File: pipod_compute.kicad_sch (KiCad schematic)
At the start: 2 parts

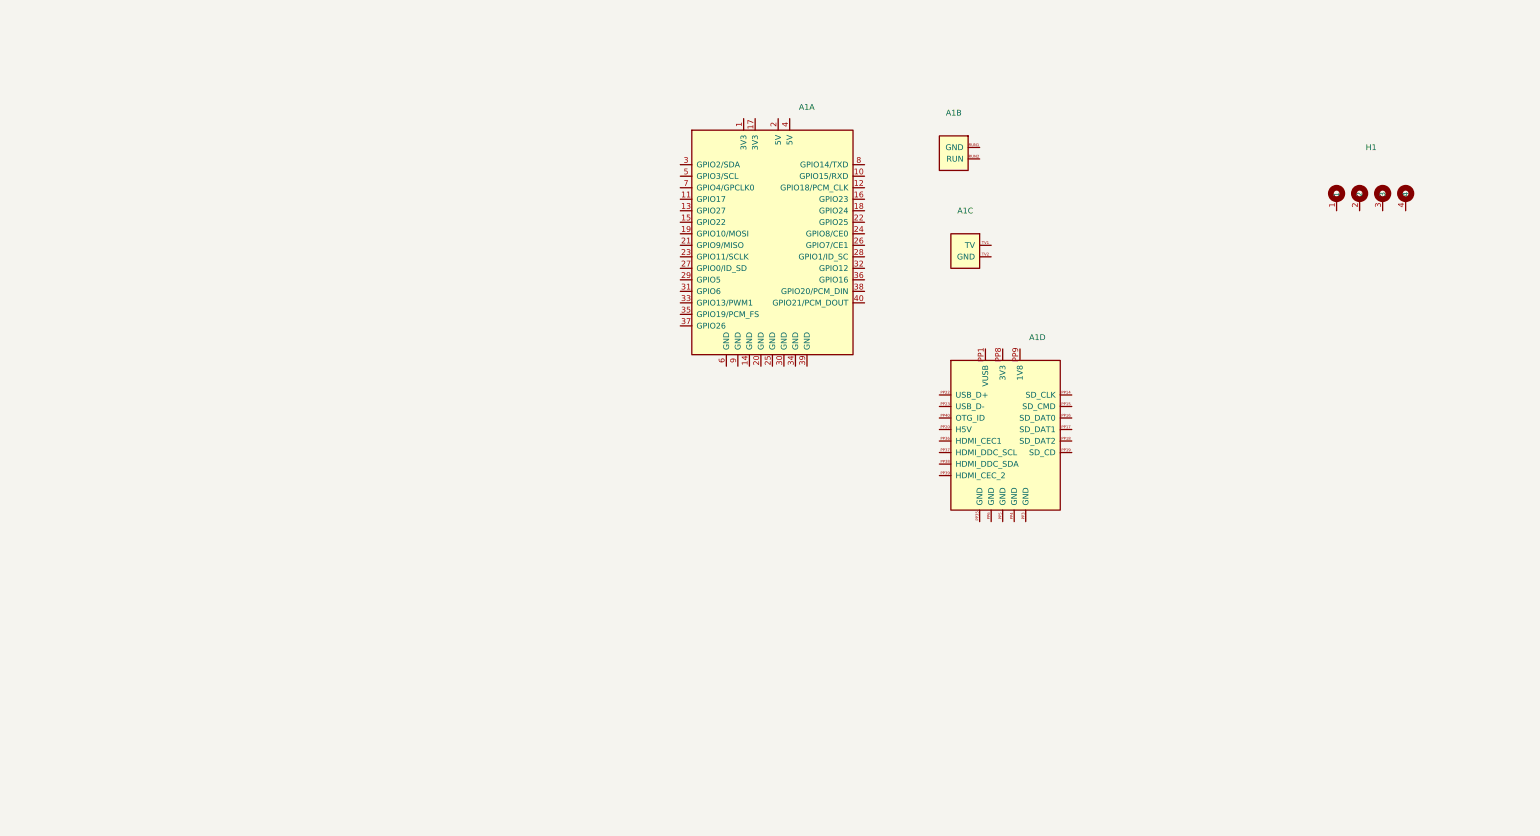
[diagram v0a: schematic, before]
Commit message: layout: cleanup silkscreen, add bootloader buttons
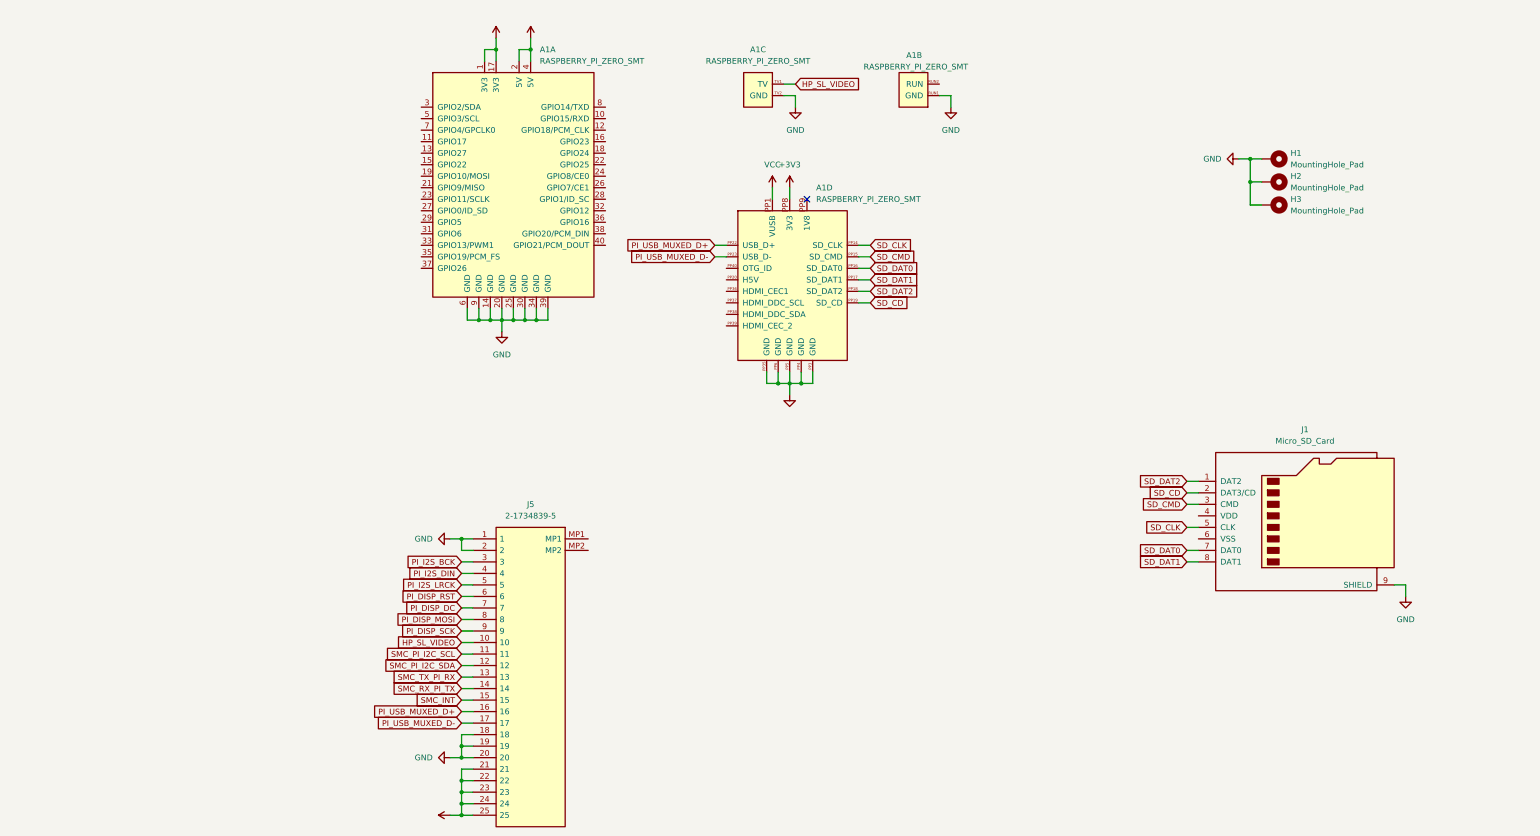
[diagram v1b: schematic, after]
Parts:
- removed H1: (no value), symbol pipod_hw:MountingHole_PiPod
- added H1, H2, H3: MountingHole_Pad, MountingHole:MountingHole_2.2mm_M2_DIN965_Pad, symbol Mechanical:MountingHole_Pad
- added J1: Micro_SD_Card, Gigahawk:microSD_HC_Hirose_DM3AT-SF-PEJM5, symbol Connector:Micro_SD_Card
- added J5: 2-1734839-5, Gigahawk:217348395, symbol gigahawk:2-1734839-5
- A1: value (none) -> RASPBERRY_PI_ZERO_SMT; footprint (none) -> Gigahawk:RASPI_ZERO_1_3_SMT_LOW_PROFILE
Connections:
- net HP_SL_VIDEO: now reaches A1.TV1 (TV)
- net HP_SL_VIDEO: now also J5.10
- net GND: now reaches A1.TV2 (GND)
- net GND: now also A1.14 (GND), A1.20 (GND), A1.25 (GND), A1.30 (GND), A1.34 (GND), A1.39 (GND), A1.6 (GND), A1.9 (GND), A1.PP3 (GND), A1.PP35 (GND), A1.PP4 (GND), A1.PP5 (GND), A1.PP6 (GND), A1.RUN1 (GND), H1.1, H2.1, H3.1, J1.9 (SHIELD), J5.1, J5.18, J5.19, J5.2, J5.20
- net VCC: now reaches A1.PP1 (VUSB)
- net VCC: now also A1.2 (5V), A1.4 (5V), J5.21, J5.22, J5.23, J5.24, J5.25
- net SD_CLK: now reaches A1.PP14 (SD_CLK)
- net SD_CLK: now also J1.5 (CLK)
- net SD_CMD: now reaches A1.PP15 (SD_CMD)
- net SD_CMD: now also J1.3 (CMD)
- net SD_DAT0: now reaches A1.PP16 (SD_DAT0)
- net SD_DAT0: now also J1.7 (DAT0)
- net SD_DAT1: now reaches A1.PP17 (SD_DAT1)
- net SD_DAT1: now also J1.8 (DAT1)
- net SD_DAT2: now reaches A1.PP18 (SD_DAT2)
- net SD_DAT2: now also J1.1 (DAT2)
- net SD_CD: now reaches A1.PP19 (SD_CD)
- net SD_CD: now also J1.2 (DAT3/CD)
- net PI_USB_MUXED_D+: now reaches A1.PP22 (USB_D+)
- net PI_USB_MUXED_D+: now also J5.16
- net PI_USB_MUXED_D-: now reaches A1.PP23 (USB_D-)
- net PI_USB_MUXED_D-: now also J5.17
- net +3V3: now reaches A1.PP8 (3V3)
- net +3V3: now also A1.1 (3V3), A1.17 (3V3)
- new net PI_DISP_DC: J5.7
- new net PI_DISP_MOSI: J5.8
- new net PI_DISP_RST: J5.6
- new net PI_DISP_SCK: J5.9
- new net PI_I2S_BCK: J5.3
- new net PI_I2S_DIN: J5.4
- new net PI_I2S_LRCK: J5.5
- new net SMC_INT: J5.15
- new net SMC_PI_I2C_SCL: J5.11
- new net SMC_PI_I2C_SDA: J5.12
- new net SMC_RX_PI_TX: J5.14
- new net SMC_TX_PI_RX: J5.13
- no-connect marks 0 -> 1
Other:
- moved on the sheet: A1A, A1B, A1C, A1D

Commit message: compute: finish layout and routing
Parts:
- added C1: (no value), symbol Device:C_Small
- added D1: (no value), symbol Device:LED
- added J?: S7041-42R, Gigahawk:S7041-42R, symbol gigahawk:S7041-42R
- added J?: (no value), symbol gigahawk:S7041-42R
- added R1, R2: (no value), symbol Device:R_Small
- added TP1, TP10, TP11, TP12, TP13, TP14, TP15, TP16, TP17, TP18, TP19, TP2, TP20, TP21, TP22, TP23, TP24, TP3, TP4, TP5, TP6, TP7, TP8, TP9: TestPoint, TestPoint:TestPoint_Pad_D1.5mm, symbol Connector:TestPoint
- J1: symbol Connector:Micro_SD_Card -> Connector:Micro_SD_Card_Det_Hirose_DM3AT
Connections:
- net +3V3: now also J1.4 (VDD), C1.2, R1.2, TP3.1
- net GND: now also J1.10 (DET_A), J1.11 (SHIELD), J1.6 (VSS), C1.1, J?.1, J?.1, R2.1, TP1.1; no longer J1.9 (SHIELD)
- net HP_SL_VIDEO: now also TP11.1
- net PI_DISP_DC: now also A1.18 (GPIO24), TP14.1
- net PI_DISP_MOSI: now also A1.19 (GPIO10/MOSI), TP13.1
- net PI_DISP_RST: now also A1.22 (GPIO25), TP15.1
- net PI_DISP_SCK: now also A1.23 (GPIO11/SCLK), TP12.1
- net PI_I2S_BCK: now also A1.12 (GPIO18/PCM_CLK), TP18.1
- net PI_I2S_DIN: now also A1.40 (GPIO21/PCM_DOUT), TP17.1
- net PI_I2S_LRCK: now also A1.35 (GPIO19/PCM_FS), TP16.1
- net SD_CD: now also TP23.1
- net SD_CLK: now also TP21.1
- net SD_CMD: now also TP22.1
- net SD_DAT0: now also TP20.1
- net SD_DAT1: now also TP19.1
- net SD_DAT2: now also TP24.1
- net SMC_INT: now also A1.16 (GPIO23), TP6.1
- net SMC_PI_I2C_SCL: now also A1.5 (GPIO3/SCL), TP10.1
- net SMC_PI_I2C_SDA: now also A1.3 (GPIO2/SDA), TP9.1
- net SMC_RX_PI_TX: now also A1.8 (GPIO14/TXD), J5.13, TP8.1; no longer J5.14
- net SMC_TX_PI_RX: now also A1.10 (GPIO15/RXD), J5.14, TP7.1; no longer J5.13
- net VCC: now also TP2.1; no longer A1.PP1 (VUSB)
- net at A1.11 (GPIO17): now also D1.2 (A), TP4.1
- net SD_DET: now reaches A1.29 (GPIO5)
- net SD_DET: now also J1.9 (DET_B), R1.1, TP5.1
- new net: D1.1 (K), R2.2
- no-connect marks 1 -> 15
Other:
- moved on the sheet: A1A, A1B, A1C, A1D

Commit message: ci: prepare files for CI
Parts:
- C1: value (none) -> 10u; footprint (none) -> Capacitor_SMD:C_0805_2012Metric
- D1: value (none) -> GRN; footprint (none) -> LED_SMD:LED_0805_2012Metric
- J2: renamed from J?; value (none) -> S7041-42R; footprint (none) -> Gigahawk:S7041-42R
- R1: value (none) -> 10k; footprint (none) -> Resistor_SMD:R_0805_2012Metric
- R2: value (none) -> 470R; footprint (none) -> Resistor_SMD:R_0805_2012Metric
- gave numbers to parts that had none: 1
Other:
- note added: "Mounting Holes"
- note added: "Shielding Clips"
- title: (none) -> piPod Compute Board
- moved on the sheet: J2, J3

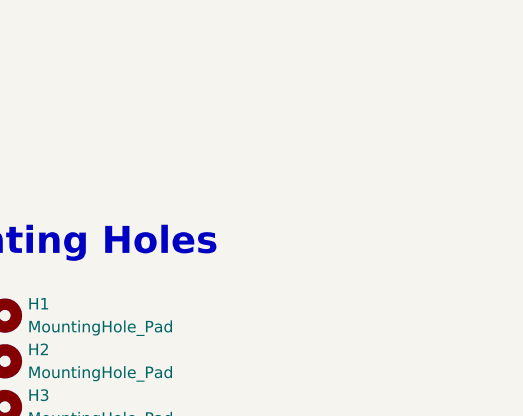
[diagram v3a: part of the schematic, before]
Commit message: layout: add OSHW logo, change version text to masked copper
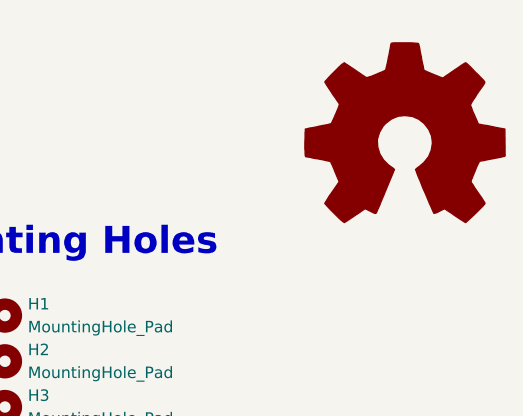
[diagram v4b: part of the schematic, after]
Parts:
- added LOGO1: (no value), symbol Graphic:Logo_Open_Hardware_Large
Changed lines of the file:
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@@
     (pin "1")
+  )
+  (symbol (lib_id "Graphic:Logo_Open_Hardware_Large") (at 267.97 27.94 0) (unit 1)
+    (in_bom yes) (on_board yes) (fields_autoplaced)
+    (property "Reference" "LOGO1" (id 0) (at 267.97 15.24 0)
+      (effects (font (size 1.27 1.27)) hide)
+    )
+    (property "Value" "" (id 1) (at 267.97 38.1 0)
+      (effects (font (size 1.27 1.27)) hide)
+    )
+    (property "Footprint" "" (id 2) (at 267.97 27.94 0)
+      (effects (font (size 1.27 1.27)) hide)
+    )
+    (property "Datasheet" "~" (id 3) (at 267.97 27.94 0)
+      (effects (font (size 1.27 1.27)) hide)
+    )
   )
   (symbol (lib_id "Device:R_Small") (at 27.94 43.18 90) (unit 1)
@@
       (reference "J5") (unit 1) (value "2-1734839-5") (footprint "Gigahawk:217348395")
     )
+    (path "/2dc8ec45-12c1-425a-8d7d-7071080501b5"
+      (reference "LOGO1") (unit 1) (value "Logo_Open_Hardware_Large") (footprint "Gigahawk:OSHW-Logo2_9.8x8mm_Mask")
+    )
     (path "/ea380145-c77c-4482-81f2-b2fdbe1fe607"

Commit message: compute: fill out bom columns
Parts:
- J1: Digikey Part (none) -> HR1964CT-ND; Digikey Price/Stock (none) -> https://www.digikey.ca/en/products/detail/hirose-electric-c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; JLC Part (none) -> Extended Part; LCSC Part (none) -> C114218; Manufacturer (none) -> Hirose Electric Co Ltd; Manufacturer Part (none) -> DM3AT-SF-PEJM5; Mouser Part (none) -> 798-DM3AT-SF-PEJM5; Mouser Price/Stock (none) -> https://www.mouser.ca/ProductDetail/Hirose-Connector/DM3AT-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
- LOGO1: value (none) -> Logo_Open_Hardware_Large; footprint (none) -> Gigahawk:OSHW-Logo2_9.8x8mm_Mask
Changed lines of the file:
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@@
       (effects (font (size 1.27 1.27)) hide)
     )
-    (property "Value" "" (id 1) (at 267.97 38.1 0)
-      (effects (font (size 1.27 1.27)) hide)
-    )
-    (property "Footprint" "" (id 2) (at 267.97 27.94 0)
+    (property "Value" "Logo_Open_Hardware_Large" (id 1) (at 267.97 38.1 0)
+      (effects (font (size 1.27 1.27)) hide)
+    )
+    (property "Footprint" "Gigahawk:OSHW-Logo2_9.8x8mm_Mask" (id 2) (at 267.97 27.94 0)
       (effects (font (size 1.27 1.27)) hide)
     )
@@
       (effects (font (size 1.27 1.27)) hide)
     )
+    (property "Description" "10 (8 + 2) Position Card Connector Secure Digital - microSD™ Surface Mount, Right Angle Gold" (id 4) (at 228.6 125.73 0)
+      (effects (font (size 1.27 1.27)) hide)
+    )
+    (property "Digikey Part" "HR1964CT-ND" (id 5) (at 228.6 125.73 0)
+      (effects (font (size 1.27 1.27)) hide)
+    )
+    (property "Digikey Price/Stock" "https://www.digikey.ca/en/products/detail/hirose-electric-co-ltd/DM3AT-SF-PEJM5/2533565" (id 6) (at 228.6 125.73 0)
+      (effects (font (size 1.27 1.27)) hide)
+    )
+    (property "JLC Part" "Extended Part" (id 7) (at 228.6 125.73 0)
+      (effects (font (size 1.27 1.27)) hide)
+    )
+    (property "LCSC Part" "C114218" (id 8) (at 228.6 125.73 0)
+      (effects (font (size 1.27 1.27)) hide)
+    )
+    (property "Manufacturer" "Hirose Electric Co Ltd" (id 9) (at 228.6 125.73 0)
+      (effects (font (size 1.27 1.27)) hide)
+    )
+    (property "Manufacturer Part" "DM3AT-SF-PEJM5" (id 10) (at 228.6 125.73 0)
+      (effects (font (size 1.27 1.27)) hide)
+    )
+    (property "Mouser Part" "798-DM3AT-SF-PEJM5" (id 11) (at 228.6 125.73 0)
+      (effects (font (size 1.27 1.27)) hide)
+    )
+    (property "Mouser Price/Stock" "https://www.mouser.ca/ProductDetail/Hirose-Connector/DM3AT-SF-PEJM5?qs=LZSZKJVF%252B2WTDKp%252BR7IYAQ%3D%3D" (id 12) (at 228.6 125.73 0)
+      (effects (font (size 1.27 1.27)) hide)
+    )

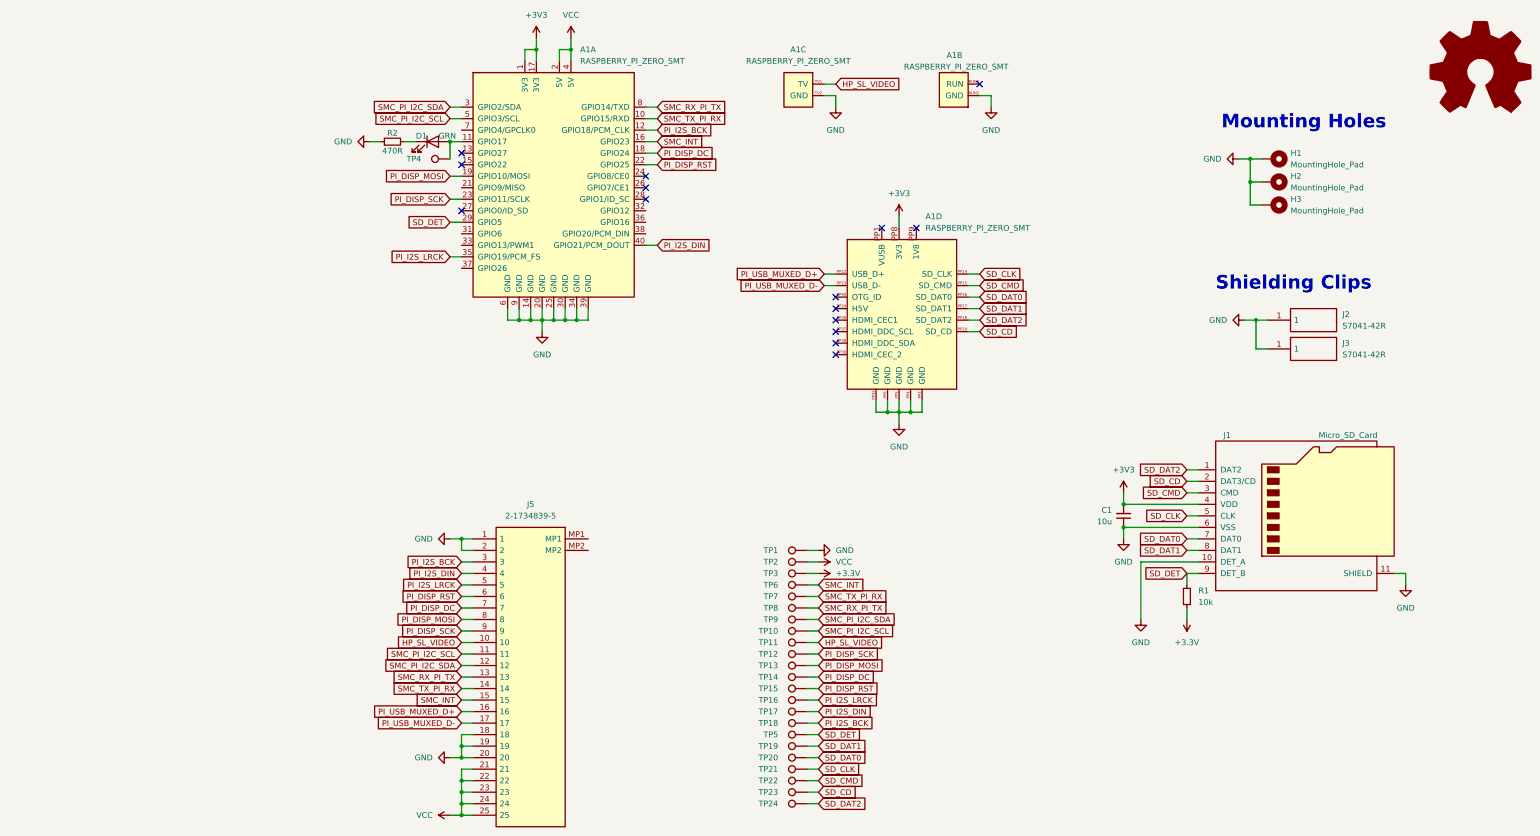
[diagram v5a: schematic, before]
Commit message: feature: add hardware ID resistors
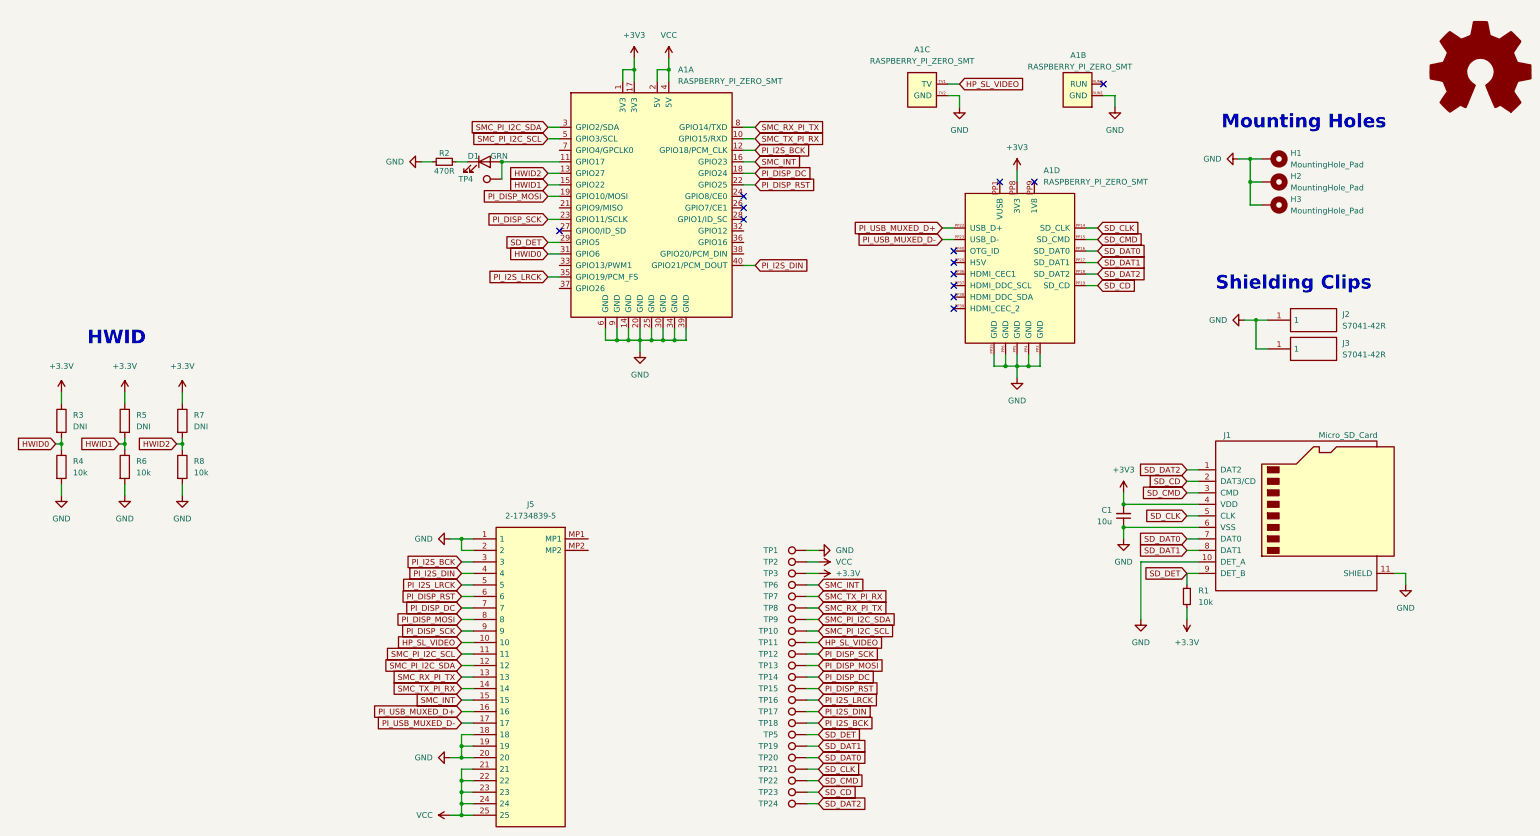
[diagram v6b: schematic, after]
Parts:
- added R3, R5, R7: DNI, symbol Device:R
- added R4, R6, R8: 10k, symbol Device:R
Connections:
- net +3V3: now also R3.1, R5.1, R7.1
- net GND: now also R4.2, R6.2, R8.2
- net HWID2: now reaches A1.13 (GPIO27)
- net HWID2: now also R7.2, R8.1
- net HWID1: now reaches A1.15 (GPIO22)
- net HWID1: now also R5.2, R6.1
- net HWID0: now reaches A1.31 (GPIO6)
- net HWID0: now also R3.2, R4.1
- no-connect marks 15 -> 13
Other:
- note added: "HWID"
- moved on the sheet: A1A, A1B, A1C, A1D, D1, R2, TP4
